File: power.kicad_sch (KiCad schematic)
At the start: 38 parts, among them Q1 DMN3008SFG, Q2 DMN3008SFG, U1 AP33771, U2 AP62150WU

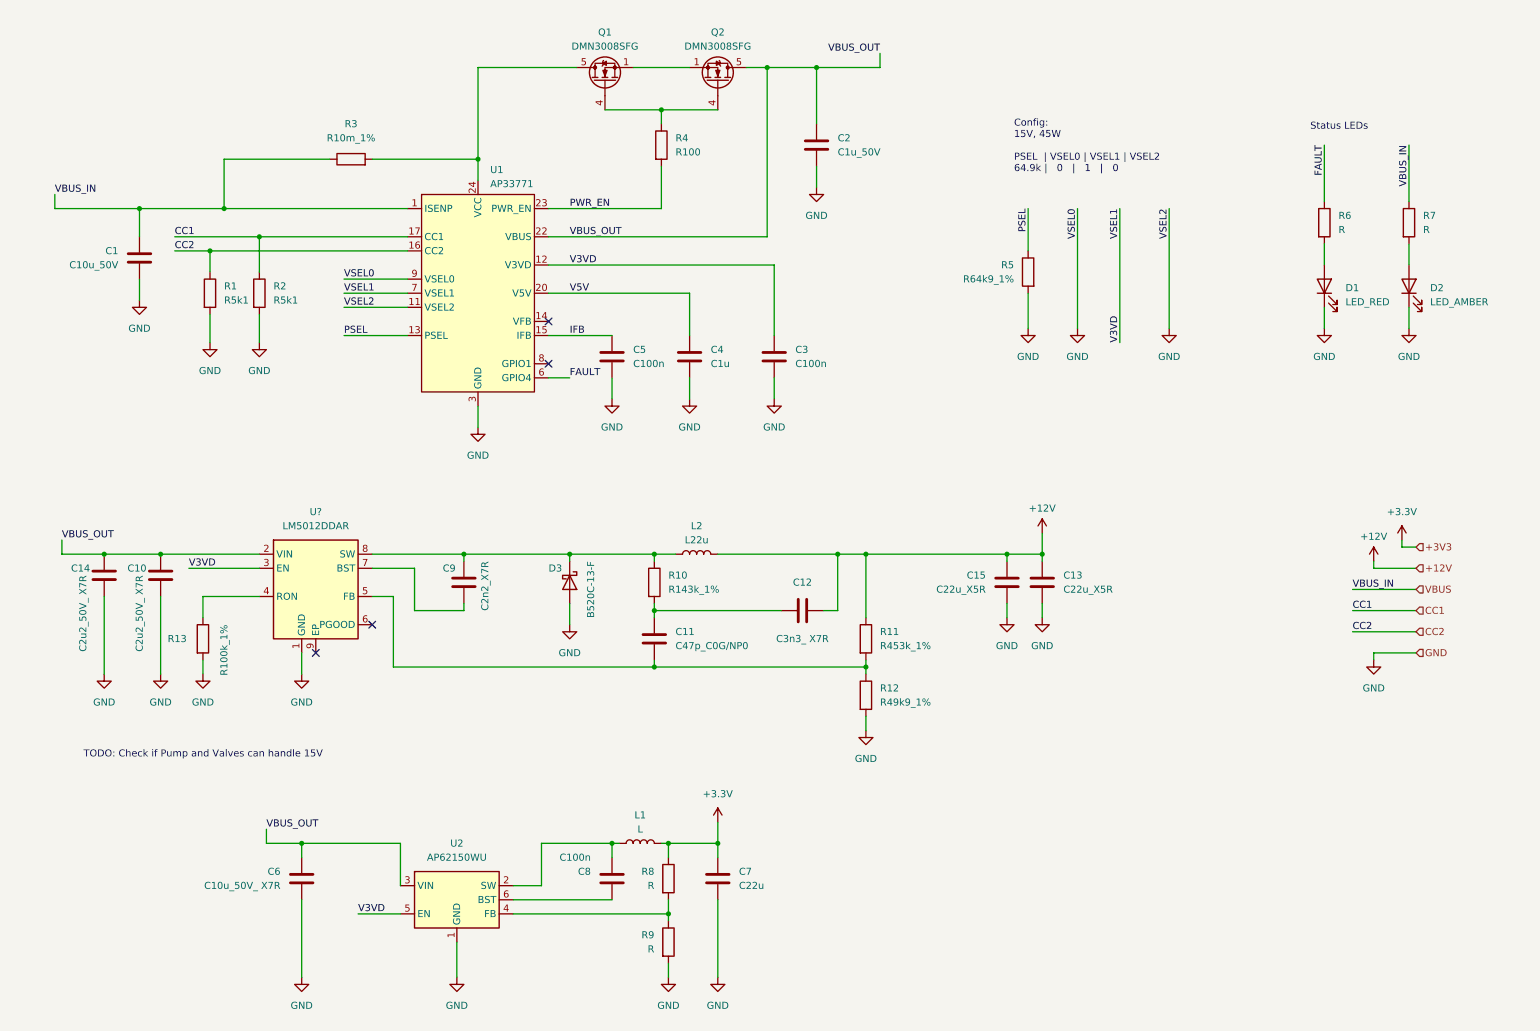
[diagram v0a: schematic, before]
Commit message: Remove 12V buck converter and power rail
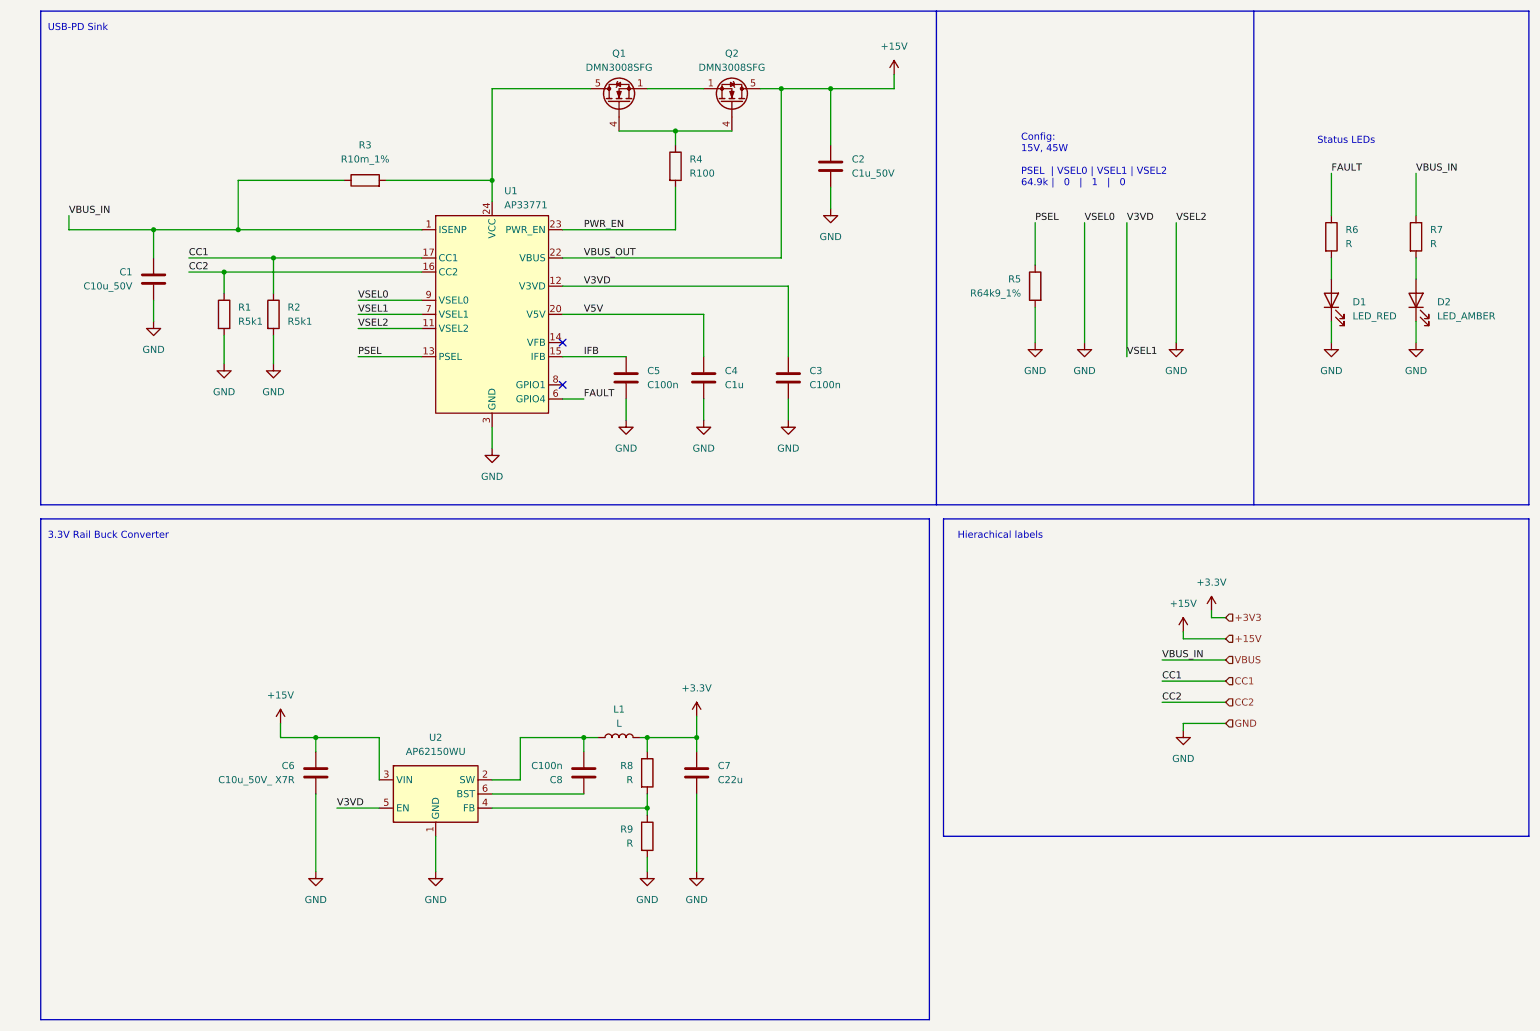
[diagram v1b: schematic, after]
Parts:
- removed C10, C14: C2u2_50V_ X7R, symbol Device:C
- removed C11: C47p_C0G/NP0, symbol Device:C
- removed C12: C3n3_ X7R, symbol Device:C
- removed C13, C15: C22u_X5R, symbol Device:C
- removed C9: C2n2_X7R, symbol Device:C
- removed D3: B520C-13-F, Diode_SMD:D_SMC, symbol Device:D_Schottky
- removed L2: L22u, symbol Device:L
- removed R10: R143k_1%, symbol Device:R
- removed R11: R453k_1%, symbol Device:R
- removed R12: R49k9_1%, symbol Device:R
- removed R13: R100k_1%, symbol Device:R
- removed U?: LM5012DDAR, Package_SO:SOIC-8-1EP_3.9x4.9mm_P1.27mm_EP2.95x4.9mm_Mask2.71x3.4mm_ThermalVias, symbol project:LM5012DDAR
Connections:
- net VBUS_OUT renamed +15V
- no-connect marks 4 -> 2
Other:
- note added: "3.3V Rail Buck Converter"
- note added: "Hierachical labels"
- note added: "USB-PD Sink"
- note removed: "TODO: Check if Pump and Valves can handle 15V"
- moved on the sheet: C1, C2, C3, C4, C5, C6, C7, C8, D1, D2, L1, Q1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
